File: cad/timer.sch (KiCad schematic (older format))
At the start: 17 parts, among them J1 Motor, J2 Pot, Q1 S9012, Q2 S9013, Q3 S9012, U1 ATMEGA328P-PU, U2 LM393, U3 L293D, Y1 AB38T-32.768kHz

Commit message: CAD files for first PCB attempt
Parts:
- added J4: Prog, Pin_Headers:Pin_Header_Straight_1x03_Pitch2.54mm, symbol Conn_01x03
- BT1, J1: footprint Pin_Headers:Pin_Header_Straight_1x02_Pitch1.00mm -> Pin_Headers:Pin_Header_Straight_1x02_Pitch2.54mm
- C1: value 47p -> 47pF
- C2, C3: value 15p -> 15pF
- J2: footprint Pin_Headers:Pin_Header_Straight_1x03_Pitch1.00mm -> Pin_Headers:Pin_Header_Straight_1x03_Pitch2.54mm
- LS1: value PSR-36N08A-JQ -> Speaker; footprint Pin_Headers:Pin_Header_Straight_1x02_Pitch1.00mm -> Pin_Headers:Pin_Header_Straight_1x02_Pitch2.54mm
- Q1, Q2, Q3: footprint TO_SOT_Packages_THT:TO-92_Molded_Narrow -> TO_SOT_Packages_THT:TO-92_Inline_Narrow_Oval
- R1: value 1M -> 1MΩ
- R2: value 47k -> 47kΩ
- R3: value 10k -> 10kΩ
- Y1: value AB38T-32.768kHz -> 32.768kHz
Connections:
- net at U1.1 ((PCINT14/~RESET~)PC6): now also J4.1 (Pin_1)
- net at U1.2 ((PCINT16/RXD)PD0): now also J4.2 (Pin_2)
- net at U1.3 ((PCINT17/TXD)PD1): now also J4.3 (Pin_3)
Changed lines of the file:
@@
 P 2400 1300
 F 0 "R1" V 2480 1300 50  0000 C CNN
-F 1 "1M" V 2400 1300 50  0000 C CNN
+F 1 "1MΩ" V 2400 1300 50  0000 C CNN
 F 2 "Resistors_THT:R_Axial_DIN0207_L6.3mm_D2.5mm_P10.16mm_Horizontal" V 2330 1300 50  0001 C CNN
 F 3 "" H 2400 1300 50  0001 C CNN
@@
 P 2850 1550
 F 0 "R2" V 2930 1550 50  0000 C CNN
-F 1 "47k" V 2850 1550 50  0000 C CNN
+F 1 "47kΩ" V 2850 1550 50  0000 C CNN
 F 2 "Resistors_THT:R_Axial_DIN0207_L6.3mm_D2.5mm_P10.16mm_Horizontal" V 2780 1550 50  0001 C CNN
 F 3 "" H 2850 1550 50  0001 C CNN
@@
 F 0 "Q1" H 6597 3360 50  0000 L CNN
 F 1 "S9012" H 6453 3276 50  0000 L CNN
-F 2 "TO_SOT_Packages_THT:TO-92_Molded_Narrow" H 6900 3025 50  0001 L CIN
+F 2 "TO_SOT_Packages_THT:TO-92_Inline_Narrow_Oval" H 6900 3025 50  0001 L CIN
 F 3 "" H 6700 3100 50  0001 L CNN
 	1    6700 3100
@@
 P 6350 3100
 F 0 "R3" V 6430 3100 50  0000 C CNN
-F 1 "10k" V 6350 3100 50  0000 C CNN
+F 1 "10kΩ" V 6350 3100 50  0000 C CNN
 F 2 "Resistors_THT:R_Axial_DIN0207_L6.3mm_D2.5mm_P10.16mm_Horizontal" V 6280 3100 50  0001 C CNN
 F 3 "" H 6350 3100 50  0001 C CNN
@@
 P 2450 3800
 F 0 "C1" H 2475 3900 50  0000 L CNN
-F 1 "47p" H 2475 3700 50  0000 L CNN
+F 1 "47pF" H 2475 3700 50  0000 L CNN
 F 2 "Capacitors_THT:C_Disc_D5.0mm_W2.5mm_P2.50mm" H 2488 3650 50  0001 C CNN
 F 3 "" H 2450 3800 50  0001 C CNN
@@
 P 5300 5600
 F 0 "Y1" H 5300 5750 50  0000 C CNN
-F 1 "AB38T-32.768kHz" H 5300 5450 50  0000 C CNN
+F 1 "32.768kHz" H 5300 5450 50  0000 C CNN
 F 2 "Crystals:Crystal_C38-LF_d3.0mm_l8.0mm_Vertical" H 5300 5600 50  0001 C CNN
 F 3 "http://www.abracon.com/Resonators/AB38T.pdf" H 5300 5600 50  0001 C CNN
@@
 P 5050 6000
 F 0 "C2" H 5075 6100 50  0000 L CNN
-F 1 "15p" H 5075 5900 50  0000 L CNN
+F 1 "15pF" H 5075 5900 50  0000 L CNN
 F 2 "Capacitors_THT:C_Disc_D5.0mm_W2.5mm_P2.50mm" H 5088 5850 50  0001 C CNN
 F 3 "" H 5050 6000 50  0001 C CNN
@@
 P 5550 6000
 F 0 "C3" H 5575 6100 50  0000 L CNN
-F 1 "15p" H 5575 5900 50  0000 L CNN
+F 1 "15pF" H 5575 5900 50  0000 L CNN
 F 2 "Capacitors_THT:C_Disc_D5.0mm_W2.5mm_P2.50mm" H 5588 5850 50  0001 C CNN
 F 3 "" H 5550 6000 50  0001 C CNN
@@
 F 0 "Q3" H 5850 1875 50  0000 L CNN
 F 1 "S9012" H 5850 1800 50  0000 L CNN
-F 2 "TO_SOT_Packages_THT:TO-92_Molded_Narrow" H 5850 1725 50  0001 L CIN
+F 2 "TO_SOT_Packages_THT:TO-92_Inline_Narrow_Oval" H 5850 1725 50  0001 L CIN
 F 3 "" H 5650 1800 50  0001 L CNN
 	1    5650 1800
@@
 F 0 "Q2" H 5850 1225 50  0000 L CNN
 F 1 "S9013" H 5850 1150 50  0000 L CNN
-F 2 "TO_SOT_Packages_THT:TO-92_Molded_Narrow" H 5850 1075 50  0001 L CIN
+F 2 "TO_SOT_Packages_THT:TO-92_Inline_Narrow_Oval" H 5850 1075 50  0001 L CIN
 F 3 "" H 5650 1150 50  0001 L CNN
 	1    5650 1150
@@
 P 6700 1500
 F 0 "LS1" H 6750 1725 50  0000 R CNN
-F 1 "PSR-36N08A-JQ" H 6750 1650 50  0000 R CNN
-F 2 "Pin_Headers:Pin_Header_Straight_1x02_Pitch1.00mm" H 6700 1300 50  0001 C CNN
+F 1 "Speaker" H 6750 1650 50  0000 R CNN
+F 2 "Pin_Headers:Pin_Header_Straight_1x02_Pitch2.54mm" H 6700 1300 50  0001 C CNN
 F 3 "" H 6690 1450 50  0001 C CNN
 	1    6700 1500
@@
 F 0 "J1" H 7750 3700 50  0000 C CNN
 F 1 "Motor" H 7750 3400 50  0000 C CNN
-F 2 "Pin_Headers:Pin_Header_Straight_1x02_Pitch1.00mm" H 7750 3600 50  0001 C CNN
+F 2 "Pin_Headers:Pin_Header_Straight_1x02_Pitch2.54mm" H 7750 3600 50  0001 C CNN
 F 3 "" H 7750 3600 50  0001 C CNN
 	1    7750 3600
@@
 F 0 "J2" H 5450 2700 50  0000 C CNN
 F 1 "Pot" H 5450 2300 50  0000 C CNN
-F 2 "Pin_Headers:Pin_Header_Straight_1x03_Pitch1.00mm" H 5450 2500 50  0001 C CNN
+F 2 "Pin_Headers:Pin_Header_Straight_1x03_Pitch2.54mm" H 5450 2500 50  0001 C CNN
 F 3 "" H 5450 2500 50  0001 C CNN
 	1    5450 2500
@@
 F 0 "BT1" H 3700 6300 50  0000 L CNN
 F 1 "Battery" H 3700 6200 50  0000 L CNN
-F 2 "Pin_Headers:Pin_Header_Straight_1x02_Pitch1.00mm" V 3600 6260 50  0001 C CNN
+F 2 "Pin_Headers:Pin_Header_Straight_1x02_Pitch2.54mm" V 3600 6260 50  0001 C CNN
 F 3 "" V 3600 6260 50  0001 C CNN
 	1    3600 6200
@@
 	1    0    0    -1
 $EndComp
+$Comp
+L Conn_01x03 J4
+U 1 1 59BFF28A
+P 5300 4500
+F 0 "J4" H 5300 4700 50  0000 C CNN
+F 1 "Prog" H 5300 4300 50  0000 C CNN
+F 2 "Pin_Headers:Pin_Header_Straight_1x03_Pitch2.54mm" H 5300 4500 50  0001 C CNN
+F 3 "" H 5300 4500 50  0001 C CNN
+	1    5300 4500
+	1    0    0    -1
+$EndComp
+Wire Wire Line
+	4500 4400 5100 4400
+Wire Wire Line
+	4500 4550 4700 4550
+Wire Wire Line
+	4700 4550 4700 4500
+Wire Wire Line
+	4700 4500 5100 4500
+Wire Wire Line
+	4500 4650 4700 4650
+Wire Wire Line
+	4700 4650 4700 4600
+Wire Wire Line
+	4700 4600 5100 4600
 $EndSCHEMATC

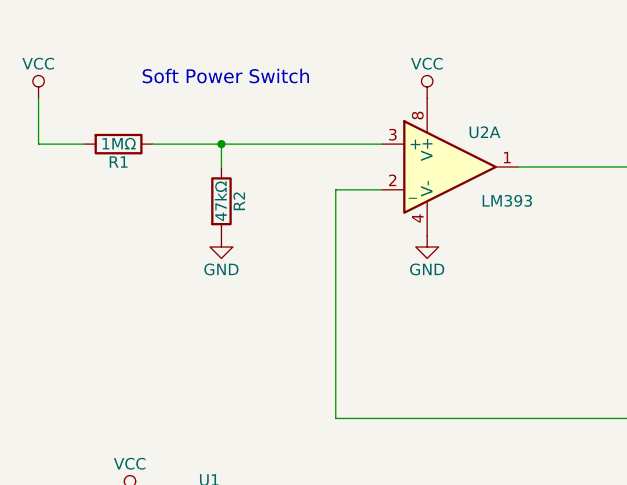
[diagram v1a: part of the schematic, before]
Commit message: CAD changes for off stop size change
The soft power switch needs a 68k instead of a 47k resistor now.
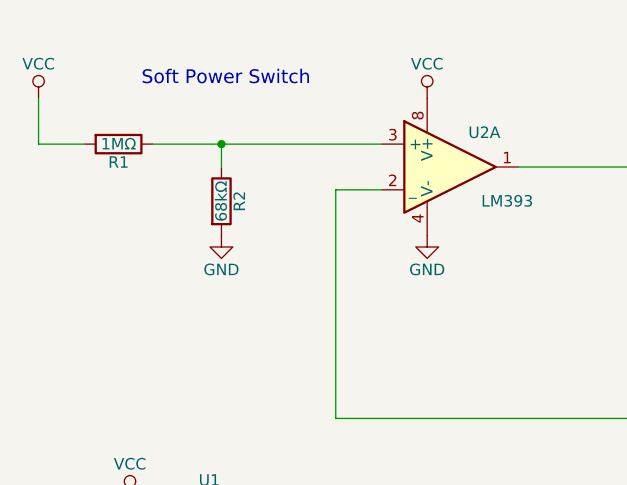
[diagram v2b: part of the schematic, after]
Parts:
- R2: value 47kΩ -> 68kΩ
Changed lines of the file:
@@
 P 2850 1550
 F 0 "R2" V 2930 1550 50  0000 C CNN
-F 1 "47kΩ" V 2850 1550 50  0000 C CNN
+F 1 "68kΩ" V 2850 1550 50  0000 C CNN
 F 2 "Resistors_THT:R_Axial_DIN0207_L6.3mm_D2.5mm_P10.16mm_Horizontal" V 2780 1550 50  0001 C CNN
 F 3 "" H 2850 1550 50  0001 C CNN

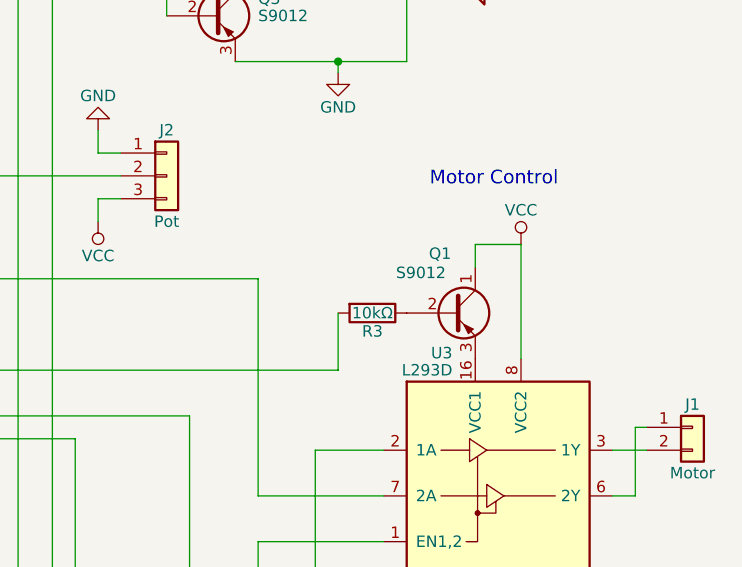
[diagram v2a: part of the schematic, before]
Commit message: More reliable motor controller switch
The previous resistor/transistor combo wasn't reliable
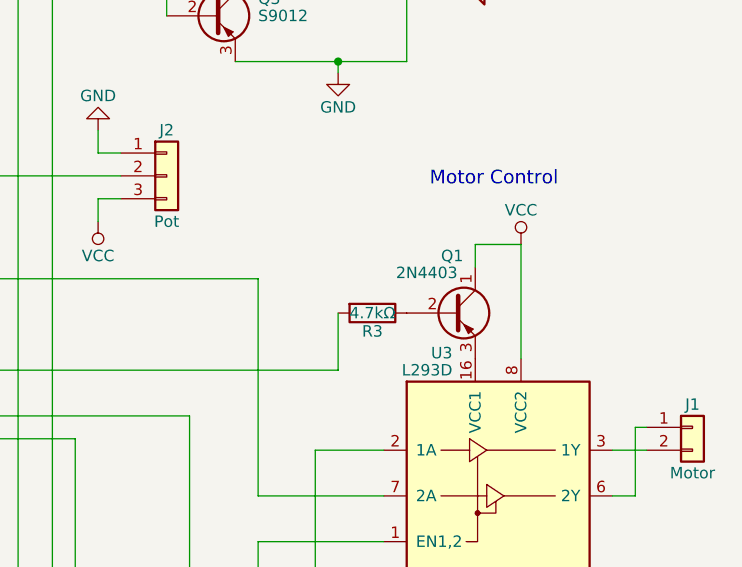
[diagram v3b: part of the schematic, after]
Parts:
- Q1: value S9012 -> 2N4403
- R3: value 10kΩ -> 4.7kΩ
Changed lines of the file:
@@
 U 1 1 59BEF6C4
 P 6700 3100
-F 0 "Q1" H 6597 3360 50  0000 L CNN
-F 1 "S9012" H 6453 3276 50  0000 L CNN
+F 0 "Q1" H 6650 3350 50  0000 L CNN
+F 1 "2N4403" H 6453 3276 50  0000 L CNN
 F 2 "TO_SOT_Packages_THT:TO-92_Inline_Narrow_Oval" H 6900 3025 50  0001 L CIN
 F 3 "" H 6700 3100 50  0001 L CNN
@@
 P 6350 3100
 F 0 "R3" V 6430 3100 50  0000 C CNN
-F 1 "10kΩ" V 6350 3100 50  0000 C CNN
+F 1 "4.7kΩ" V 6350 3100 50  0000 C CNN
 F 2 "Resistors_THT:R_Axial_DIN0207_L6.3mm_D2.5mm_P10.16mm_Horizontal" V 6280 3100 50  0001 C CNN
 F 3 "" H 6350 3100 50  0001 C CNN

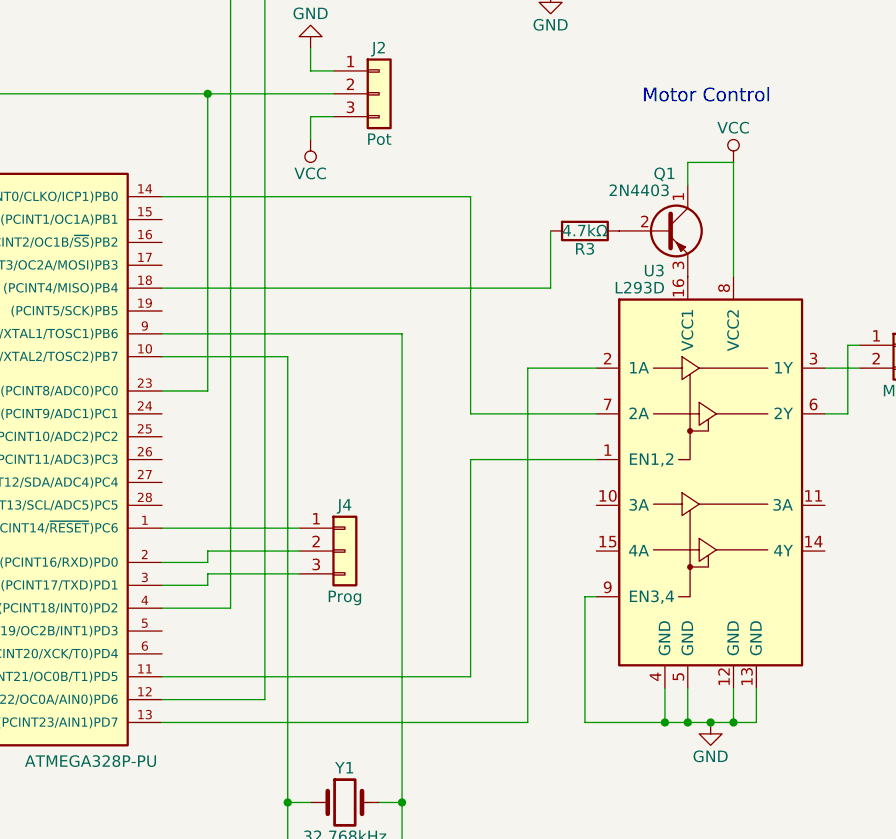
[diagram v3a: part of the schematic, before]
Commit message: Remove separate power switch for motor controller
This was causing all sorts of problems, just go back to the original,
simpler setup where the enable pin and logic supply voltage pin are
connected (thus only powering the chip when enabling the motor).
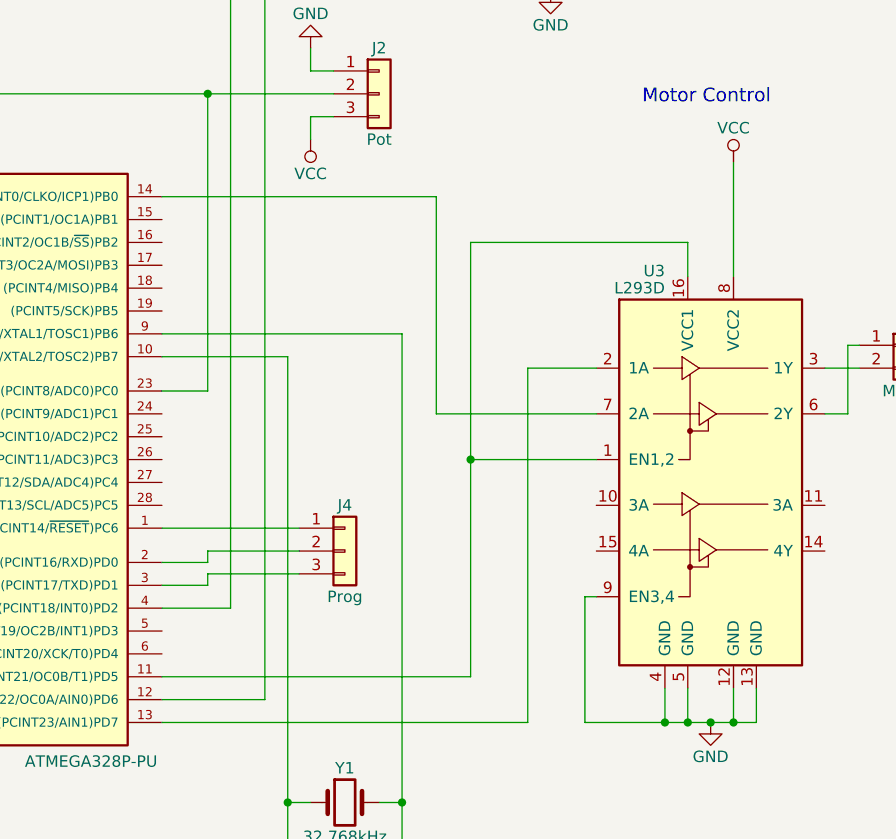
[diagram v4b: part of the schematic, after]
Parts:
- removed Q1: 2N4403, TO_SOT_Packages_THT:TO-92_Inline_Narrow_Oval, symbol BC327
- removed R3: 4.7kΩ, Resistors_THT:R_Axial_DIN0207_L6.3mm_D2.5mm_P10.16mm_Horizontal, symbol R
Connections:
- net at U1.11 ((PCINT21/OC0B/T1)PD5), U3.1 (EN1,2): now also U3.16 (VCC1)
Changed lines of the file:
@@
-$EndComp
-$Comp
-L BC327 Q1
-U 1 1 59BEF6C4
-P 6700 3100
-F 0 "Q1" H 6650 3350 50  0000 L CNN
-F 1 "2N4403" H 6453 3276 50  0000 L CNN
-F 2 "TO_SOT_Packages_THT:TO-92_Inline_Narrow_Oval" H 6900 3025 50  0001 L CIN
-F 3 "" H 6700 3100 50  0001 L CNN
-	1    6700 3100
-	1    0    0    -1
 $EndComp
 $Comp
@@
 $EndComp
 $Comp
-L R R3
-U 1 1 59BF0740
-P 6350 3100
-F 0 "R3" V 6430 3100 50  0000 C CNN
-F 1 "4.7kΩ" V 6350 3100 50  0000 C CNN
-F 2 "Resistors_THT:R_Axial_DIN0207_L6.3mm_D2.5mm_P10.16mm_Horizontal" V 6280 3100 50  0001 C CNN
-F 3 "" H 6350 3100 50  0001 C CNN
-	1    6350 3100
-	0    1    1    0
-$EndComp
-$Comp
 L GND #PWR06
 U 1 1 59BF0888
@@
 Connection ~ 6700 5250
 Wire Wire Line
-	6800 2900 6800 2800
-Wire Wire Line
-	6800 2800 7000 2800
-Wire Wire Line
 	7000 2800 7000 3300
 Wire Wire Line
@@
 	6100 3700 6400 3700
 Wire Wire Line
-	4500 2950 5850 2950
-Wire Wire Line
-	5850 2950 5850 3900
-Wire Wire Line
-	5850 3900 6400 3900
-Wire Wire Line
-	4500 5050 5850 5050
-Wire Wire Line
-	5850 5050 5850 4100
+	5700 2950 5700 3900
+Wire Wire Line
+	5850 5050 4500 5050
+Wire Wire Line
+	5850 3150 5850 5050
 Wire Wire Line
 	5850 4100 6400 4100
-Wire Wire Line
-	4500 3350 6200 3350
-Wire Wire Line
-	6200 3350 6200 3100
 Wire Wire Line
 	2450 2850 2450 3250
@@
 Wire Wire Line
 	4700 4600 5100 4600
+Wire Wire Line
+	4500 2950 5700 2950
+Wire Wire Line
+	5700 3900 6400 3900
+Wire Wire Line
+	5850 3150 6800 3150
+Wire Wire Line
+	6800 3150 6800 3300
+Connection ~ 5850 4100
 $EndSCHEMATC

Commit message: Updated schematic and PCB design
- Increased hole size to 3mm
- Removed motor controller on/off switch (Q1 and R3)
- Swap transistor footprint for one that's easier to solder
- Reroute with FreeRoutingNew
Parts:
- Q2, Q3: footprint TO_SOT_Packages_THT:TO-92_Inline_Narrow_Oval -> TO_SOT_Packages_THT:TO-92_Inline_Wide
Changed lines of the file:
@@
 F 0 "Q3" H 5850 1875 50  0000 L CNN
 F 1 "S9012" H 5850 1800 50  0000 L CNN
-F 2 "TO_SOT_Packages_THT:TO-92_Inline_Narrow_Oval" H 5850 1725 50  0001 L CIN
+F 2 "TO_SOT_Packages_THT:TO-92_Inline_Wide" H 5850 1725 50  0001 L CIN
 F 3 "" H 5650 1800 50  0001 L CNN
 	1    5650 1800
@@
 F 0 "Q2" H 5850 1225 50  0000 L CNN
 F 1 "S9013" H 5850 1150 50  0000 L CNN
-F 2 "TO_SOT_Packages_THT:TO-92_Inline_Narrow_Oval" H 5850 1075 50  0001 L CIN
+F 2 "TO_SOT_Packages_THT:TO-92_Inline_Wide" H 5850 1075 50  0001 L CIN
 F 3 "" H 5650 1150 50  0001 L CNN
 	1    5650 1150
